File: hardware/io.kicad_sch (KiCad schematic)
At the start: 25 parts, among them J10 Cable Servomoteur JST, J5 SeedStudio 110990037, J6 72454-010VLF, J7 DF3A-5P-2DS, J8 DF3A-5P-2DS, J9 B2B-XH-2, Q2 TPH2R506PL,L1Q, U4 PCA9306DP, U5 74AHC1G126

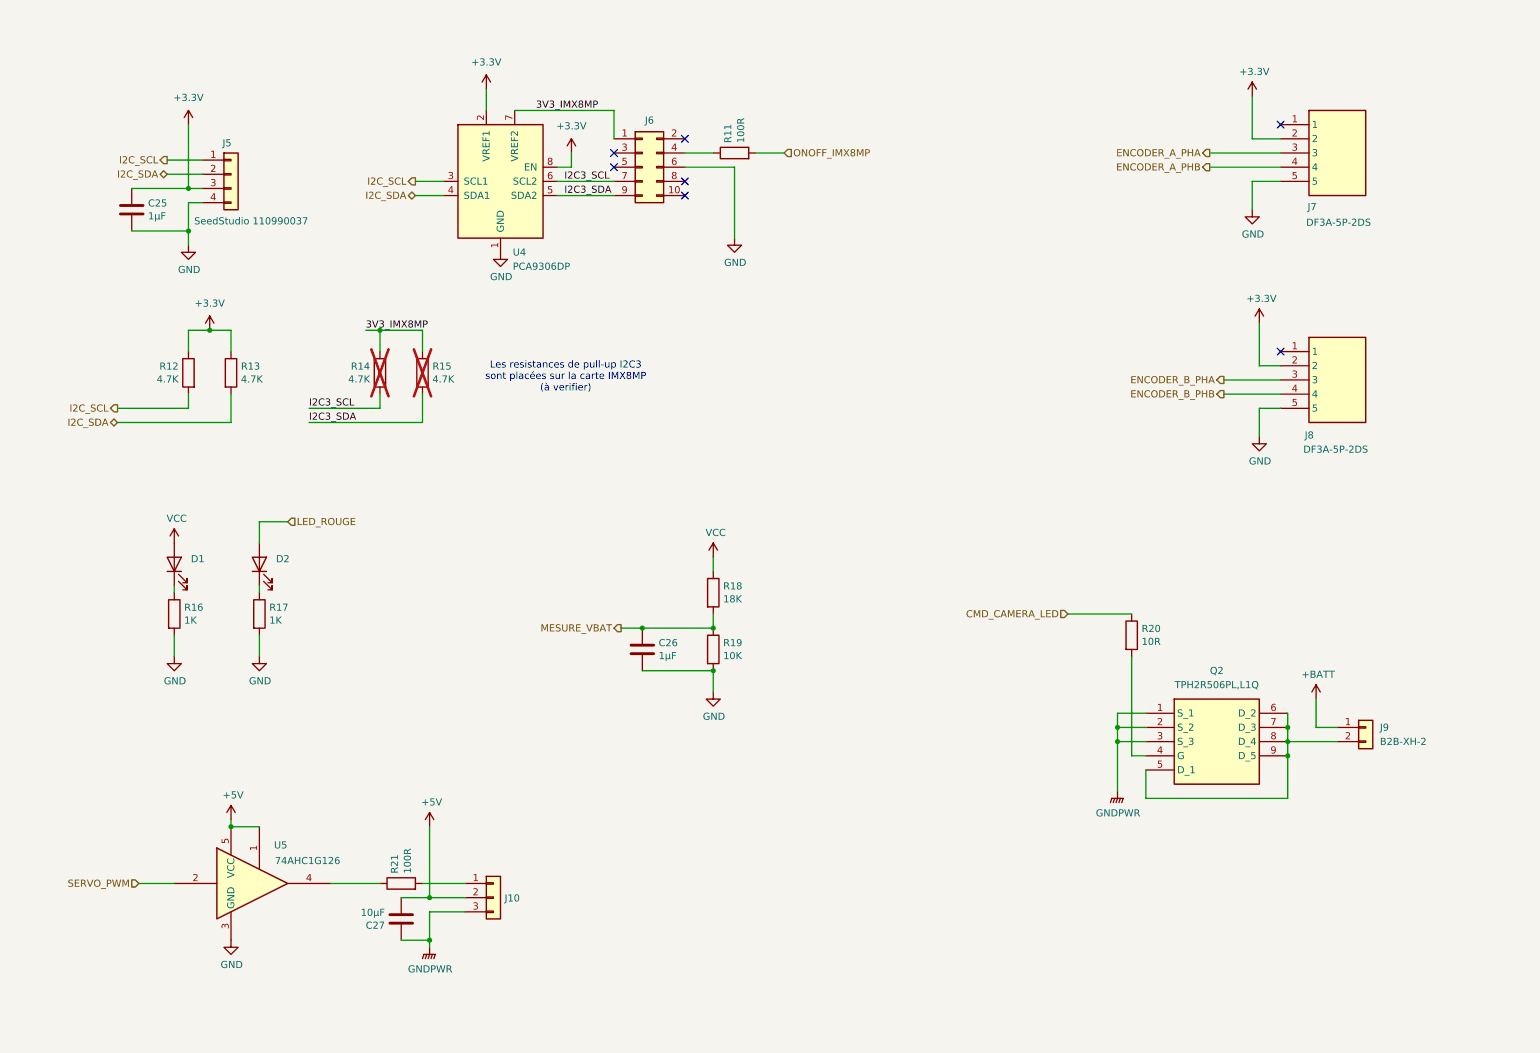
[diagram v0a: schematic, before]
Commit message: Wip carte alamk pwr 2.0 prete pour tirage
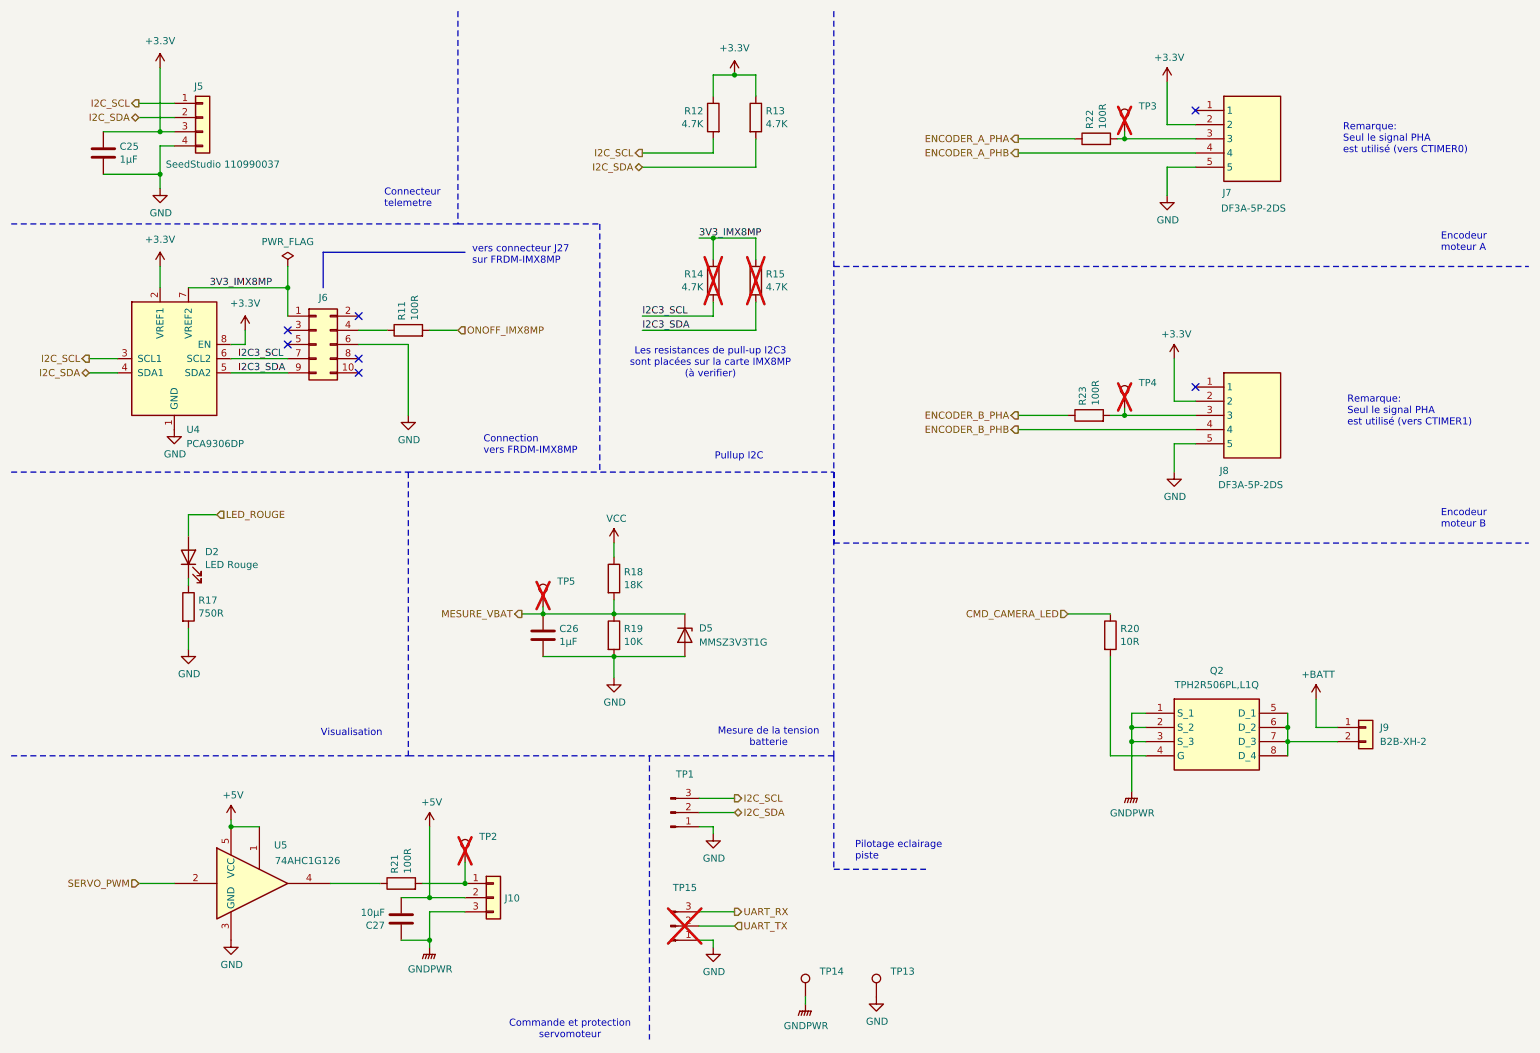
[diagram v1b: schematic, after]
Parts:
- removed D1: LED Bleue, LED_SMD:LED_0805_2012Metric, symbol Device:LED
- removed R16: 1K, Resistor_SMD:R_0805_2012Metric, symbol Device:R
- added D5: MMSZ3V3T1G, Diode_SMD:D_SOD-123, symbol Device:D_Zener
- added R22, R23: 100R, Resistor_SMD:R_0805_2012Metric, symbol Device:R
- added TP1, TP15: Conn_01x03_Pin, Connector_PinHeader_2.54mm:PinHeader_1x03_P2.54mm_Vertical, symbol Connector:Conn_01x03_Pin
- added TP13, TP14, TP2, TP3, TP4, TP5: TestPoint, Connector_PinHeader_2.54mm:PinHeader_1x01_P2.54mm_Vertical, symbol Connector:TestPoint
- J10: footprint Connector_Wire:SolderWirePad_1x03_P3.175mm_Drill1mm -> Connector_Wire:SolderWire-0.5sqmm_1x03_P4.8mm_D0.9mm_OD2.3mm
- J7, J8: footprint SHDRRA5W60P0X200_1X5_1200X720X530P -> DF3A-5P-2DS:SHDRRA5W60P0X200_1X5_1200X720X530P
- J9: footprint (none) -> Connector_JST:JST_XH_B2B-XH-A_1x02_P2.50mm_Vertical
- R17: value 1K -> 750R; Part Number RT0805BRD071KL -> RT0805BRD07750RL
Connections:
- net ENCODER_A_PHA: now also R22.1; no longer J7.3
- net ENCODER_B_PHA: now also R23.1; no longer J8.3
- net GND: now also D5.2 (A), TP1.1 (Pin_1), TP13.1, TP15.1 (Pin_1)
- net GNDPWR: now also TP14.1
- net I2C_SCL: now also TP1.3 (Pin_3)
- net I2C_SDA: now also TP1.2 (Pin_2)
- net MESURE_VBAT: now also D5.1 (K), TP5.1
- net at J10.1 (Pin_1), R21.2: now also TP2.1
- net at J9.2 (Pin_2), Q2.5 (D_1), Q2.6 (D_2)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: no longer Q2.9 (D_5)
- new net: J8.3, R23.2, TP4.1
- new net: J7.3, R22.2, TP3.1
- new net UART_RX: TP15.3 (Pin_3)
- new net UART_TX: TP15.2 (Pin_2)
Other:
- note added: "Commande et protection servomoteur"
- note added: "Connecteur telemetre"
- note added: "Connection vers FRDM-IMX8MP"
- note added: "Encodeur moteur A"
- note added: "Encodeur moteur B"
- note added: "Mesure de la tension batterie"
- note added: "Pilotage eclairage piste"
- note added: "Pullup I2C"
- note added: "Remarque: Seul le signal PHA est utilisé (vers CTIMER0)"
- note added: "Remarque: Seul le signal PHA est utilisé (vers CTIMER1)"
- note added: "Visualisation"
- note added: "vers connecteur J27 sur FRDM-IMX8MP"
- moved on the sheet: C25, C26, D2, J5, J6, J7, J8, R11, R12, R13, R14, R15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
